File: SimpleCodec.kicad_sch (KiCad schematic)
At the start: 7 parts, among them J1 RPI_ADC, J2 RP_GPIO

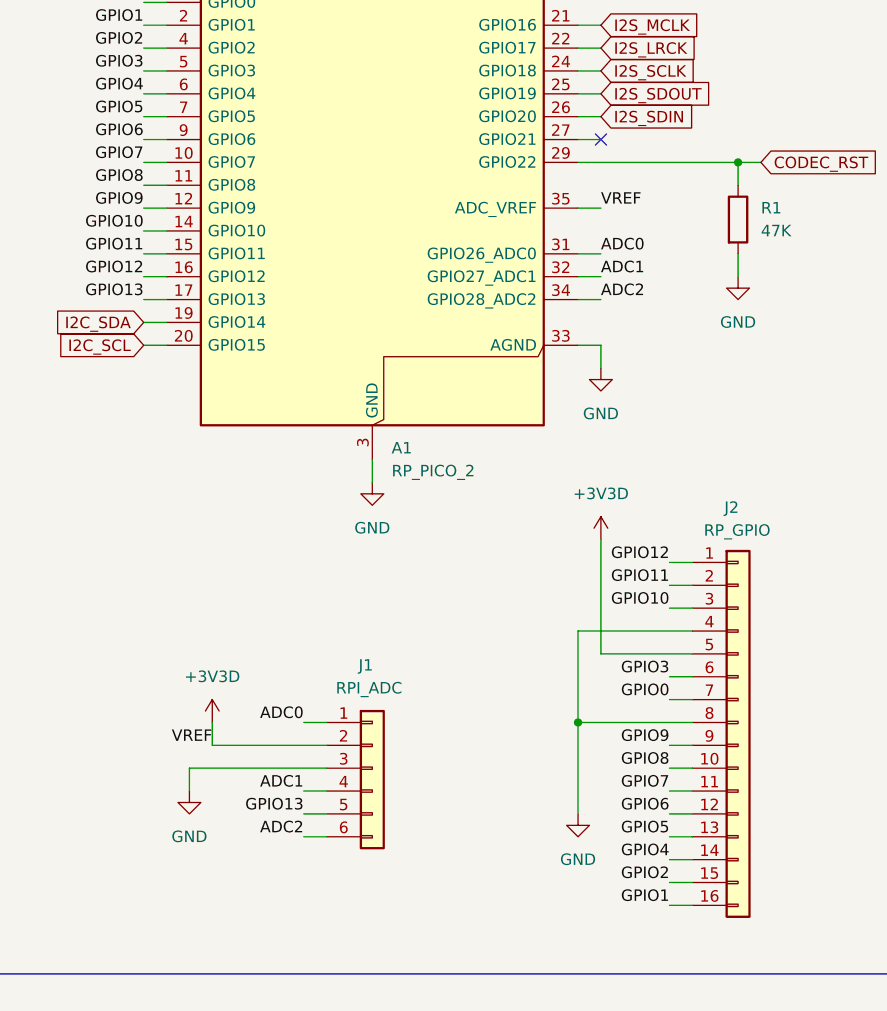
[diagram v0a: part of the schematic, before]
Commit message: Layout and power supply filtering
Updated the board layout.
Updated the project to KiCad 10.0.
Added additional power supply filtering.
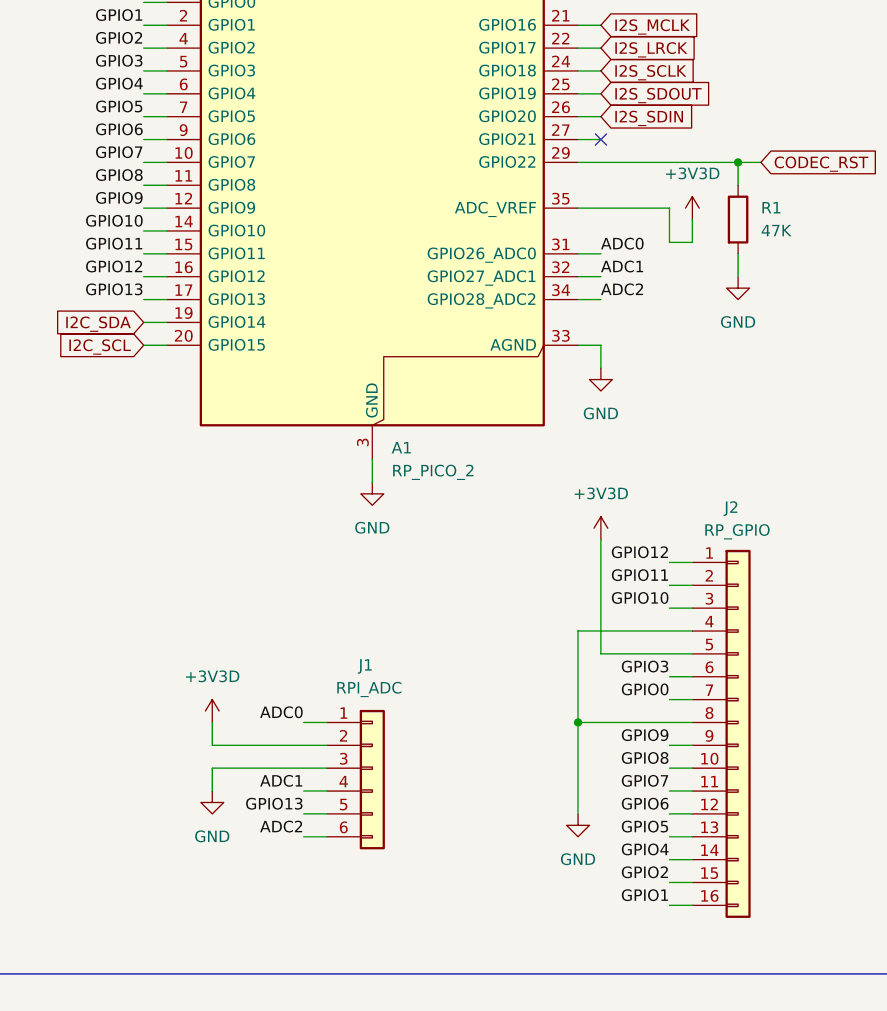
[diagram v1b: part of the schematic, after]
